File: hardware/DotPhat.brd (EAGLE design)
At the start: 30 x 65 mm, 21 parts, among them J2 RASPBERRYPI-40-PIN-GPIO_PTH, U1 ATMEGA328P-MU-QFN32, X3 S4B-ZR

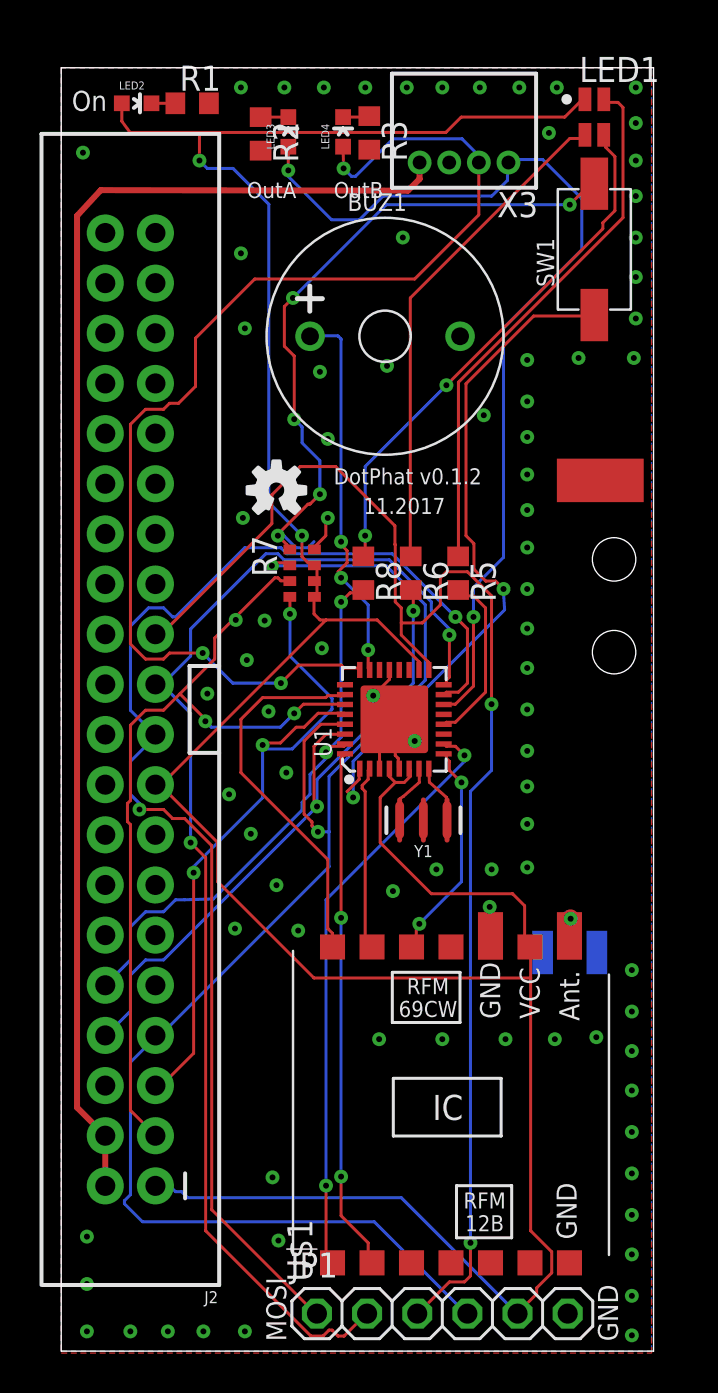
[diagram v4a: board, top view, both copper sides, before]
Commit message: Add microusb
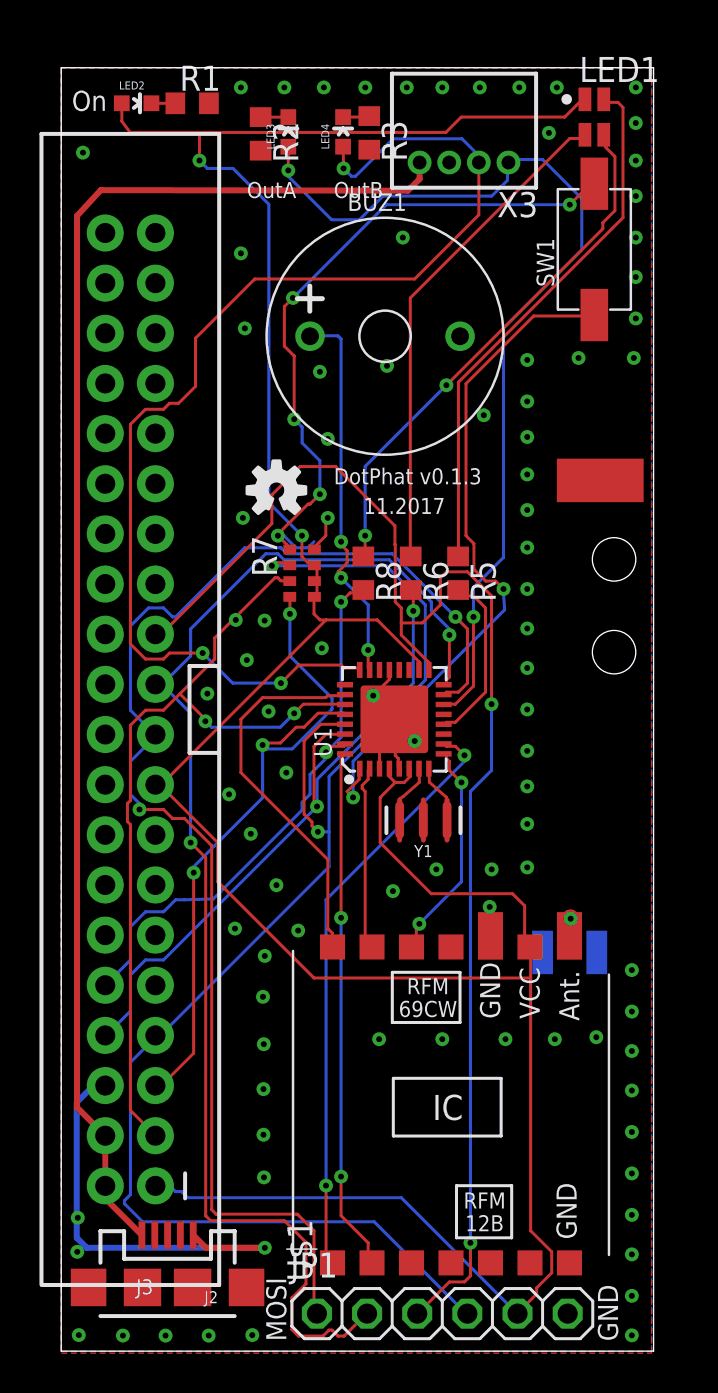
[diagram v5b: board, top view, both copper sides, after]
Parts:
- added J3: USB-MICROB, SparkFun-Retired:USB-MICROB
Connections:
- net +5V: now also J3.VBUS
- net GND: now also J3.GND, J3.MT1, J3.MT2
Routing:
- net GND: track 11.0 -> 33.3 mm, vias 84 -> 89
- net +5V: track 68.7 -> 72.0 mm
- net MISO: track 63.3 -> 66.4 mm
- net MOSI: track 65.9 -> 68.3 mm
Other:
- board text added: "DotPhat v0.1.3"
- board text removed: "DotPhat v0.1.2"
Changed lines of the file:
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@@
 <layer number="22" name="bPlace" color="7" fill="1" visible="yes" active="yes"/>
 <layer number="23" name="tOrigins" color="15" fill="1" visible="yes" active="yes"/>
-<layer number="24" name="bOrigins" color="15" fill="1" visible="no" active="yes"/>
+<layer number="24" name="bOrigins" color="15" fill="1" visible="yes" active="yes"/>
 <layer number="25" name="tNames" color="7" fill="1" visible="no" active="yes"/>
 <layer number="26" name="bNames" color="7" fill="1" visible="no" active="yes"/>
@@
 <layer number="46" name="Milling" color="3" fill="1" visible="no" active="yes"/>
 <layer number="47" name="Measures" color="7" fill="1" visible="no" active="yes"/>
-<layer number="48" name="Document" color="7" fill="1" visible="yes" active="yes"/>
+<layer number="48" name="Document" color="7" fill="1" visible="no" active="yes"/>
 <layer number="49" name="Reference" color="7" fill="1" visible="no" active="yes"/>
 <layer number="50" name="dxf" color="7" fill="1" visible="no" active="no"/>
@@
 <text x="28.2" y="0.5" size="1.016" layer="21" rot="R90">GND</text>
 <rectangle x1="25.1" y1="43" x2="29.5" y2="45.2" layer="1"/>
-<text x="13.8" y="43.9" size="0.8128" layer="21">DotPhat v0.1.2</text>
+<text x="13.8" y="43.9" size="0.8128" layer="21">DotPhat v0.1.3</text>
 <text x="15.3" y="42.4" size="0.8128" layer="21">11.2017</text>
 <rectangle x1="14" y1="28.7" x2="19.8" y2="34.9" layer="43"/>
@@
 <element name="R3" library="resistor" package="R0603" value="250Ω" x="15.6" y="61.7" rot="R270"/>
 <element name="LED4" library="SparkFun" package="LED-0603" value="" x="14.2746" y="61.7508"/>
+<element name="J3" library="SparkFun-Retired" package="USB-MICROB" value="USB-MICROB" x="5.3848" y="3.2258">
+<attribute name="PROD_ID" value="CONN-09505" x="5.3848" y="3.2258" size="1.778" layer="27" display="off"/>
+</element>
 </elements>
 <signals>
@@
 <via x="27.1" y="15.9" extent="1-16" drill="0.3"/>
 <via x="16.1" y="15.8" extent="1-16" drill="0.3"/>
-<via x="1.3" y="1" extent="1-16" drill="0.3"/>
-<via x="3.5" y="1" extent="1-16" drill="0.3"/>
-<via x="5.4" y="1" extent="1-16" drill="0.3"/>
-<via x="7.2" y="1" extent="1-16" drill="0.3"/>
-<via x="9.3" y="1" extent="1-16" drill="0.3"/>
 <via x="21.4" y="47.4" extent="1-16" drill="0.3"/>
 <via x="9.1" y="64" extent="1-16" drill="0.3"/>
@@
 <via x="24.7" y="61.7" extent="1-16" drill="0.3"/>
 <via x="1.1" y="60.7" extent="1-16" drill="0.3"/>
-<via x="1.3" y="3.4" extent="1-16" drill="0.3"/>
-<via x="1.3" y="5.8" extent="1-16" drill="0.3"/>
 <via x="17.3" y="56.4" extent="1-16" drill="0.3"/>
 <via x="9.1" y="55.6" extent="1-16" drill="0.3"/>
@@
 <via x="16.8" y="23.3" extent="1-16" drill="0.3"/>
 <via x="19" y="24.4" extent="1-16" drill="0.3"/>
-<via x="11" y="5.6" extent="1-16" drill="0.3"/>
-<via x="10.7" y="8.8" extent="1-16" drill="0.3"/>
+<via x="10.2682" y="8.8" extent="1-16" drill="0.3"/>
 <contactref element="R1" pad="2"/>
 <contactref element="R2" pad="2"/>
 <contactref element="R3" pad="2"/>
 <contactref element="X3" pad="3"/>
+<contactref element="J3" pad="MT1"/>
+<contactref element="J3" pad="MT2"/>
+<contactref element="J3" pad="GND"/>
+<wire x1="6.6848" y1="5.8758" x2="7.3282" y2="5.2324" width="0.3048" layer="1"/>
+<wire x1="7.3282" y1="5.2324" x2="10.3124" y2="5.2324" width="0.3048" layer="1"/>
+<via x="10.3124" y="5.2324" extent="1-16" drill="0.3"/>
+<wire x1="10.3124" y1="5.2324" x2="1.2954" y2="5.2324" width="0.3048" layer="16"/>
+<wire x1="1.2954" y1="5.2324" x2="0.7874" y2="5.7404" width="0.3048" layer="16"/>
+<wire x1="0.7874" y1="5.7404" x2="0.7874" y2="12.5984" width="0.3048" layer="16"/>
+<wire x1="0.7874" y1="12.5984" x2="1.639" y2="13.45" width="0.3048" layer="16"/>
+<wire x1="1.639" y1="13.45" x2="2.23" y2="13.45" width="0.3048" layer="16"/>
+<via x="9.6774" y="0.8128" extent="1-16" drill="0.3"/>
+<via x="7.4676" y="0.7874" extent="1-16" drill="0.3"/>
+<via x="5.2832" y="0.7874" extent="1-16" drill="0.3"/>
+<via x="3.1242" y="0.7874" extent="1-16" drill="0.3"/>
+<via x="0.889" y="0.8128" extent="1-16" drill="0.3"/>
+<via x="0.8128" y="5.0292" extent="1-16" drill="0.3"/>
+<via x="0.8382" y="6.7564" extent="1-16" drill="0.3"/>
+<via x="10.258" y="15.546" extent="1-16" drill="0.3"/>
+<via x="10.3088" y="20.0164" extent="1-16" drill="0.3"/>
+<via x="10.2428" y="10.959" extent="1-16" drill="0.3"/>
+<via x="10.2428" y="13.2704" extent="1-16" drill="0.3"/>
+<via x="10.2174" y="17.944" extent="1-16" drill="0.3"/>
 </signal>
 <signal name="SDA">
@@
 <wire x1="19.5072" y1="33.3756" x2="19.37" y2="33.25" width="0.1524" layer="1"/>
 <wire x1="4.7244" y1="31.242" x2="4.77" y2="31.23" width="0.1524" layer="16"/>
-<wire x1="7.62" y1="7.1628" x2="12.8016" y2="1.9812" width="0.1524" layer="1"/>
+<wire x1="12.8016" y1="1.9558" x2="12.8016" y2="1.9812" width="0.1524" layer="1"/>
 <wire x1="7.62" y1="25.6032" x2="7.62" y2="7.1628" width="0.1524" layer="1"/>
 <wire x1="6.2484" y1="26.9748" x2="7.62" y2="25.6032" width="0.1524" layer="1"/>
@@
 <via x="19.9644" y="37.1856" extent="1-16" drill="0.3"/>
 <via x="3.9624" y="27.432" extent="1-16" drill="0.3"/>
+<wire x1="7.62" y1="7.1628" x2="7.8486" y2="6.9342" width="0.1524" layer="1"/>
+<wire x1="7.8486" y1="6.9342" x2="11.9634" y2="6.9342" width="0.1524" layer="1"/>
+<wire x1="11.9634" y1="6.9342" x2="12.8016" y2="6.096" width="0.1524" layer="1"/>
+<wire x1="12.8016" y1="6.096" x2="12.8016" y2="1.9812" width="0.1524" layer="1"/>
 </signal>
 <signal name="MISO">
@@
 <wire x1="13.5636" y1="1.0668" x2="13.716" y2="1.0668" width="0.1524" layer="1"/>
 <wire x1="13.2588" y1="0.762" x2="13.5636" y2="1.0668" width="0.1524" layer="1"/>
-<wire x1="12.6492" y1="0.762" x2="13.2588" y2="0.762" width="0.1524" layer="1"/>
-<wire x1="7.3152" y1="6.096" x2="12.6492" y2="0.762" width="0.1524" layer="1"/>
-<wire x1="7.3152" y1="24.9936" x2="7.3152" y2="6.096" width="0.1524" layer="1"/>
+<wire x1="7.3152" y1="24.9936" x2="7.3152" y2="6.858" width="0.1524" layer="1"/>
 <wire x1="6.5532" y1="25.7556" x2="7.3152" y2="24.9936" width="0.1524" layer="1"/>
 <wire x1="6.5532" y1="32.3088" x2="6.5532" y2="25.7556" width="0.1524" layer="16"/>
@@
 <via x="19.6596" y="36.2712" extent="1-16" drill="0.3"/>
 <via x="6.5532" y="25.7556" extent="1-16" drill="0.3"/>
+<wire x1="7.3152" y1="6.858" x2="7.5692" y2="6.604" width="0.1524" layer="1"/>
+<wire x1="7.5692" y1="6.604" x2="11.303" y2="6.604" width="0.1524" layer="1"/>
+<wire x1="11.303" y1="6.604" x2="12.3952" y2="5.5118" width="0.1524" layer="1"/>
+<wire x1="12.3952" y1="5.5118" x2="12.3952" y2="3.4036" width="0.1524" layer="1"/>
+<wire x1="12.3952" y1="3.4036" x2="11.684" y2="2.6924" width="0.1524" layer="1"/>
+<wire x1="11.684" y1="2.6924" x2="11.684" y2="1.0922" width="0.1524" layer="1"/>
+<wire x1="11.684" y1="1.0922" x2="12.0142" y2="0.762" width="0.1524" layer="1"/>
+<wire x1="12.0142" y1="0.762" x2="13.2588" y2="0.762" width="0.1524" layer="1"/>
 </signal>
 <signal name="TXD">
@@
 <wire x1="17.557" y1="58.7746" x2="18.15" y2="59.3676" width="0.3048" layer="1"/>
 <wire x1="18.15" y1="59.3676" x2="18.15" y2="60.2" width="0.3048" layer="1"/>
+<contactref element="J3" pad="VBUS"/>
+<wire x1="4.0848" y1="5.8758" x2="2.23" y2="7.7306" width="0.3048" layer="1"/>
+<wire x1="2.23" y1="7.7306" x2="2.23" y2="8.37" width="0.3048" layer="1"/>
 </signal>
 <signal name="N$2">

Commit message: Add I2C
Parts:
- added CN1: 1X4-BIG, adafruit:1X04-BIG
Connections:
- net +3V3: now also CN1.3
- net GND: now also CN1.4
- net SCL: now also CN1.2
- net SDA: now also CN1.1
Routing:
- net SDA: track 43.0 -> 48.7 mm
- net SCL: track 35.5 -> 41.2 mm
- net +3V3: track 154.1 -> 159.6 mm
- net GND: track 33.3 -> 35.2 mm, vias 89 -> 102
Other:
- board text added: "SDA"
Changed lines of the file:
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@@
 <text x="11.4" y="0.5" size="1.016" layer="21" rot="R90">MOSI</text>
 <text x="28.2" y="0.5" size="1.016" layer="21" rot="R90">GND</text>
-<rectangle x1="25.1" y1="43" x2="29.5" y2="45.2" layer="1"/>
 <text x="13.8" y="43.9" size="0.8128" layer="21">DotPhat v0.1.3</text>
 <text x="15.3" y="42.4" size="0.8128" layer="21">11.2017</text>
@@
 <text x="9.4" y="58.4" size="0.8128" layer="21">OutA</text>
 <text x="13.8" y="58.4" size="0.8128" layer="21">OutB</text>
-<rectangle x1="25.1" y1="43" x2="29.5" y2="45.2" layer="29"/>
 <hole x="28" y="40.1" drill="2.2"/>
 <hole x="28" y="35.4" drill="2.2"/>
@@
 <text x="25.8318" y="13.5382" size="1.27" layer="22" rot="SMR0">Mihai Galos</text>
 <text x="0.5334" y="62.8142" size="1.016" layer="21">On</text>
+<rectangle x1="25.3492" y1="44.1198" x2="29.3116" y2="45.4914" layer="1"/>
+<rectangle x1="25.3492" y1="44.1198" x2="29.3116" y2="45.4914" layer="29"/>
+<text x="10.414" y="5.5372" size="1.016" layer="21" rot="R90">SDA</text>
+<text x="10.4394" y="19.1262" size="1.016" layer="21" rot="R90">GND</text>
 </plain>
 <attributes>
@@
 <attribute name="PROD_ID" value="CONN-09505" x="5.3848" y="3.2258" size="1.778" layer="27" display="off"/>
 </element>
+<element name="CN1" library="adafruit" package="1X04-BIG" value="1X4-BIG" x="9.906" y="9.7028" rot="R90"/>
 </elements>
 <signals>
@@
 <via x="16.8" y="23.3" extent="1-16" drill="0.3"/>
 <via x="19" y="24.4" extent="1-16" drill="0.3"/>
-<via x="10.2682" y="8.8" extent="1-16" drill="0.3"/>
 <contactref element="R1" pad="2"/>
 <contactref element="R2" pad="2"/>
@@
 <contactref element="J3" pad="GND"/>
 <wire x1="6.6848" y1="5.8758" x2="7.3282" y2="5.2324" width="0.3048" layer="1"/>
-<wire x1="7.3282" y1="5.2324" x2="10.3124" y2="5.2324" width="0.3048" layer="1"/>
-<via x="10.3124" y="5.2324" extent="1-16" drill="0.3"/>
-<wire x1="10.3124" y1="5.2324" x2="1.2954" y2="5.2324" width="0.3048" layer="16"/>
+<wire x1="7.3282" y1="5.2324" x2="11.2776" y2="4.9022" width="0.3048" layer="1"/>
+<via x="11.2776" y="4.9022" extent="1-16" drill="0.3"/>
+<wire x1="11.2776" y1="4.9022" x2="1.2954" y2="5.2324" width="0.3048" layer="16"/>
 <wire x1="1.2954" y1="5.2324" x2="0.7874" y2="5.7404" width="0.3048" layer="16"/>
 <wire x1="0.7874" y1="5.7404" x2="0.7874" y2="12.5984" width="0.3048" layer="16"/>
@@
 <via x="0.8128" y="5.0292" extent="1-16" drill="0.3"/>
 <via x="0.8382" y="6.7564" extent="1-16" drill="0.3"/>
-<via x="10.258" y="15.546" extent="1-16" drill="0.3"/>
-<via x="10.3088" y="20.0164" extent="1-16" drill="0.3"/>
-<via x="10.2428" y="10.959" extent="1-16" drill="0.3"/>
-<via x="10.2428" y="13.2704" extent="1-16" drill="0.3"/>
-<via x="10.2174" y="17.944" extent="1-16" drill="0.3"/>
+<via x="27.1474" y="19.3508" extent="1-16" drill="0.3"/>
+<via x="24.3458" y="56.777" extent="1-16" drill="0.3"/>
+<via x="22.771" y="55.2784" extent="1-16" drill="0.3"/>
+<via x="20.993" y="53.729" extent="1-16" drill="0.3"/>
+<via x="16.5226" y="47.7854" extent="1-16" drill="0.3"/>
+<via x="12.2554" y="56.8278" extent="1-16" drill="0.3"/>
+<via x="15.2526" y="55.2276" extent="1-16" drill="0.3"/>
+<via x="19.4436" y="57.2342" extent="1-16" drill="0.3"/>
+<via x="5.2958" y="60.6378" extent="1-16" drill="0.3"/>
+<via x="3.2892" y="60.6124" extent="1-16" drill="0.3"/>
+<via x="6.7944" y="39.3526" extent="1-16" drill="0.3"/>
+<via x="6.7598" y="41.2542" extent="1-16" drill="0.3"/>
+<via x="6.7598" y="43.1542" extent="1-16" drill="0.3"/>
+<via x="6.7598" y="45.1828" extent="1-16" drill="0.3"/>
+<via x="6.7598" y="47.2066" extent="1-16" drill="0.3"/>
+<contactref element="CN1" pad="4"/>
+<via x="12.4916" y="15.871" extent="1-16" drill="0.3"/>
+<via x="12.4916" y="13.771" extent="1-16" drill="0.3"/>
+<via x="12.4916" y="11.771" extent="1-16" drill="0.3"/>
+<via x="12.4916" y="9.771" extent="1-16" drill="0.3"/>
 </signal>
 <signal name="SDA">
@@
 <wire x1="7.3" y1="31.9" x2="7.3" y2="32" width="0.1524" layer="1"/>
 <wire x1="7.3" y1="32" x2="6.0102" y2="33.2898" width="0.1524" layer="1"/>
+<contactref element="CN1" pad="1"/>
+<wire x1="4.77" y1="10.91" x2="5.9772" y2="9.7028" width="0.1524" layer="16"/>
+<wire x1="5.9772" y1="9.7028" x2="9.906" y2="9.7028" width="0.1524" layer="16"/>
 </signal>
 <signal name="RST">
@@
 <wire x1="12.8016" y1="39.9288" x2="12.825" y2="39.8" width="0.1524" layer="1"/>
 <wire x1="12.8016" y1="18.8976" x2="23.7744" y2="18.8976" width="0.1524" layer="1"/>
-<wire x1="7.9248" y1="23.7744" x2="12.8016" y2="18.8976" width="0.1524" layer="1"/>
+<wire x1="7.9248" y1="23.7744" x2="12.5095" y2="19.1897" width="0.1524" layer="1"/>
+<wire x1="12.5095" y1="19.1897" x2="12.8016" y2="18.8976" width="0.1524" layer="1"/>
 <wire x1="7.9248" y1="25.7556" x2="7.9248" y2="23.7744" width="0.1524" layer="1"/>
 <wire x1="4.8768" y1="28.8036" x2="7.9248" y2="25.7556" width="0.1524" layer="1"/>
@@
 <wire x1="7" y1="60.3" x2="7" y2="61.622" width="0.1524" layer="1"/>
 <wire x1="7" y1="61.622" x2="6.9" y2="61.722" width="0.1524" layer="1"/>
+<contactref element="CN1" pad="3"/>
+<wire x1="9.906" y1="14.7828" x2="12.5095" y2="17.3863" width="0.1524" layer="1"/>
+<wire x1="12.5095" y1="17.3863" x2="12.5095" y2="19.1897" width="0.1524" layer="1"/>
 </signal>
 <signal name="ADCENA">
@@
 <wire x1="11.7" y1="30.5" x2="10.4" y2="30.5" width="0.1524" layer="16"/>
 <wire x1="10.4" y1="30.5" x2="10.2" y2="30.7" width="0.1524" layer="16"/>
+<contactref element="CN1" pad="2"/>
+<wire x1="4.77" y1="13.45" x2="5.9772" y2="12.2428" width="0.1524" layer="16"/>
+<wire x1="5.9772" y1="12.2428" x2="9.906" y2="12.2428" width="0.1524" layer="16"/>
 </signal>
 <signal name="PUSH">
@@
 <wire x1="15.5762" y1="62.5008" x2="15.6" y2="62.55" width="0.1524" layer="1"/>
 </signal>
+<signal name="GND1">
+<via x="6.6836" y="52.6842" extent="1-16" drill="0.3"/>
+<via x="6.6582" y="54.4826" extent="1-16" drill="0.3"/>
+<via x="6.6074" y="56.308" extent="1-16" drill="0.3"/>
+<via x="6.582" y="57.9508" extent="1-16" drill="0.3"/>
+<wire x1="6.582" y1="57.9508" x2="6.6074" y2="56.308" width="0" layer="19" extent="1-1"/>
+<wire x1="6.6582" y1="54.4826" x2="6.6074" y2="56.308" width="0" layer="19" extent="1-1"/>
+<wire x1="6.6836" y1="52.6842" x2="6.6582" y2="54.4826" width="0" layer="19" extent="1-1"/>
+</signal>
 </signals>

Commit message: Improving GND
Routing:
- net GND: vias 102 -> 117
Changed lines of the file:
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@@
 <via x="16.5" y="49.9" extent="1-16" drill="0.3"/>
 <via x="11.4" y="29.3" extent="1-16" drill="0.3"/>
-<via x="10.9" y="23.6" extent="1-16" drill="0.3"/>
+<via x="10.5444" y="23.346" extent="1-16" drill="0.3"/>
 <via x="12" y="21.3" extent="1-16" drill="0.3"/>
 <via x="16.8" y="23.3" extent="1-16" drill="0.3"/>
@@
 <via x="12.4916" y="11.771" extent="1-16" drill="0.3"/>
 <via x="12.4916" y="9.771" extent="1-16" drill="0.3"/>
+<via x="9.3508" y="49.9204" extent="1-16" drill="0.3"/>
+<via x="9.3508" y="48.0662" extent="1-16" drill="0.3"/>
+<via x="9.3762" y="45.958" extent="1-16" drill="0.3"/>
+<via x="6.6836" y="52.6842" extent="1-16" drill="0.3"/>
+<via x="6.6582" y="54.4826" extent="1-16" drill="0.3"/>
+<via x="6.6074" y="56.308" extent="1-16" drill="0.3"/>
+<via x="6.582" y="57.9508" extent="1-16" drill="0.3"/>
+<via x="9.1" y="57.505" extent="1-16" drill="0.3"/>
+<via x="15.278" y="53.221" extent="1-16" drill="0.3"/>
+<via x="18.86" y="46.7396" extent="1-16" drill="0.3"/>
+<via x="21.4254" y="45.622" extent="1-16" drill="0.3"/>
+<via x="21.4508" y="43.209" extent="1-16" drill="0.3"/>
+<via x="21.4508" y="41.6342" extent="1-16" drill="0.3"/>
+<via x="11.8398" y="24.6922" extent="1-16" drill="0.3"/>
+<via x="12.9144" y="60.4554" extent="1-16" drill="0.3"/>
 </signal>
 <signal name="SDA">
@@
 <wire x1="15.5762" y1="62.5008" x2="15.6" y2="62.55" width="0.1524" layer="1"/>
 </signal>
-<signal name="GND1">
-<via x="6.6836" y="52.6842" extent="1-16" drill="0.3"/>
-<via x="6.6582" y="54.4826" extent="1-16" drill="0.3"/>
-<via x="6.6074" y="56.308" extent="1-16" drill="0.3"/>
-<via x="6.582" y="57.9508" extent="1-16" drill="0.3"/>
-<wire x1="6.582" y1="57.9508" x2="6.6074" y2="56.308" width="0" layer="19" extent="1-1"/>
-<wire x1="6.6582" y1="54.4826" x2="6.6074" y2="56.308" width="0" layer="19" extent="1-1"/>
-<wire x1="6.6836" y1="52.6842" x2="6.6582" y2="54.4826" width="0" layer="19" extent="1-1"/>
-</signal>
 </signals>
